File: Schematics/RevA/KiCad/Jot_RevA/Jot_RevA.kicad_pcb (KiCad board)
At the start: 4 copper layers, 37 x 62.6 mm, 83 parts, among them J1 USB-C, J2 Battery, Q1 AO3400A, Q2 AO3401A, Q3 AO3400A, Q4 AO3400A, Q5 AO3400A, Q6 AO3401A, Q7 AO3400A, Q8 AO3400A, SW1 SW_Push, U1 MDBT50Q-1MV2, U10 USBLC6-2SC6, U2 MMICT3902-00-012, U3 MMICT3902-00-012, U4 W25Q256JVEIQ, U5 MCP73831T-2ACI/OT, U6 MAX17048, U7 LIS2DW12TR, U8 DRV2605LDGS, U9 TPS7A0233, Y1 32.768kHz

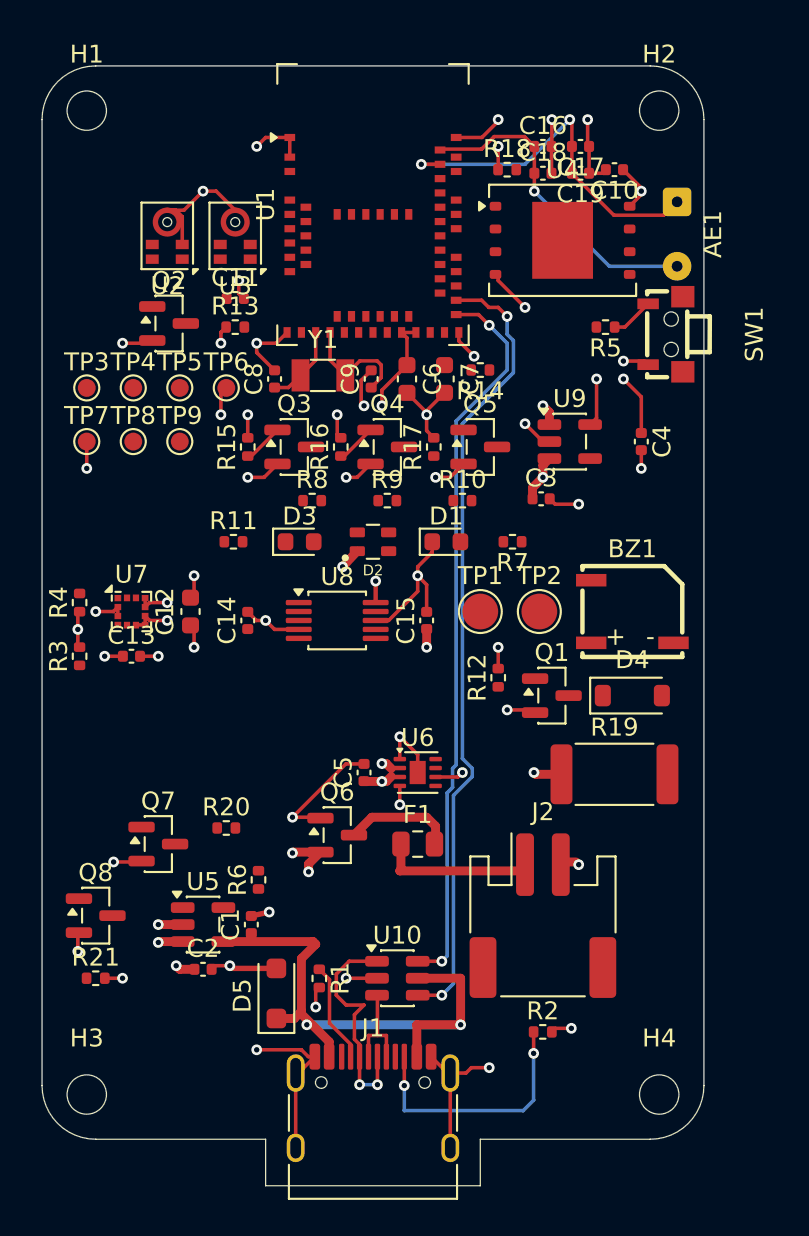
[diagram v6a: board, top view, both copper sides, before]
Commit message: Rev A layout complete: final routing and layout review fixes
- J2 is now two solder-wire holes (battery leads soldered): the JST-PH
  side-entry header is 5.5 mm tall and would not fit the 12.8 mm case.
  Removed from the JLCPCB BOM; BOM, architecture doc and case notes updated.
- LED drive pins re-assigned to match the transistor order:
  P1.08 red, P0.11 green, P0.12 blue. Pin list updated.
- No via drilled inside an SMD pad; no top-layer signal or via beside the
  crystal; 5 V branch removed from the power layer under the USB pair.
- R19 off the battery, C11 next to the mic, short ground vias at the
  module and decoupling capacitors, clean reset route.
- Silkscreen labels at 1.0 mm, battery + / - marked; zones refilled.
- DRC clean, board matches schematic, ERC clean.
- Case: 0.4 mm pocket over SW1, lip 0.8 mm.
- Architecture draft 7.
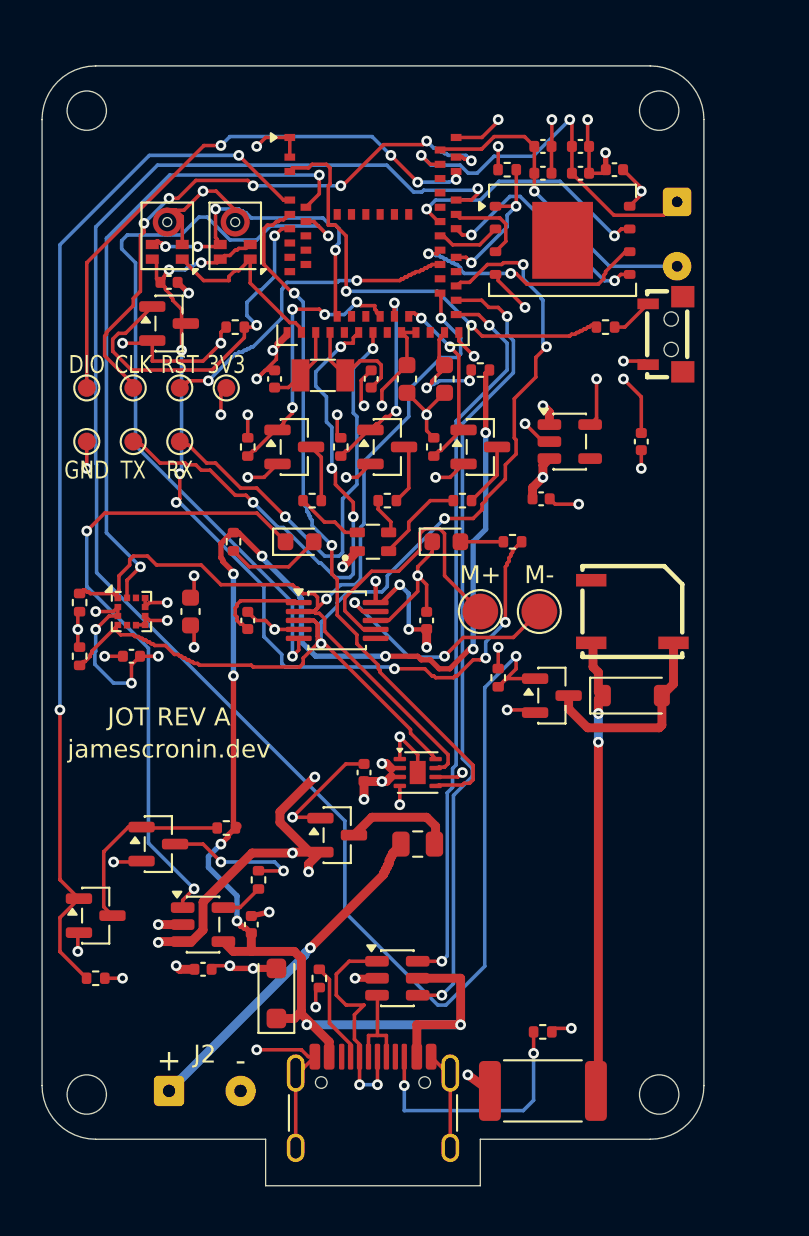
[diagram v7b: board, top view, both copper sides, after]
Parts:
- J2: value Battery -> Battery wires; footprint Connector_JST:JST_PH_S2B-PH-SM4-TB_1x02-1MP_P2.00mm_Horizontal -> Connector_Wire:SolderWire-0.15sqmm_1x02_P4mm_D0.5mm_OD1.5mm
- moved J2 23.1 mm to (88.6, 127.3)
- moved R19 18.1 mm to (109.5, 127.3)
- moved C11 3.81 mm to (88.6, 82.1)
- turned R11 to 90 degrees
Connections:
- U1 pad 25: LED_B -> LED_R
- U1 pad 27: LED_R -> LED_G
- U1 pad 29: LED_G -> LED_B
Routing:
- net BUZZER_PWM: track 0.00 -> 102.5 mm, vias 0 -> 2
- net I2C_SDA: track 0.00 -> 65.7 mm, vias 0 -> 4
- net VBUS: track 32.4 -> 91.2 mm, vias 2 -> 10
- net CHG_INHIBIT: track 0.00 -> 58.5 mm, vias 0 -> 2
- net I2C_SCL: track 0.00 -> 55.0 mm, vias 0 -> 2
- net /Audio/MIC_VDD: track 0.00 -> 51.7 mm, vias 0 -> 8
- net HAPTIC_EN: track 0.00 -> 43.1 mm, vias 0 -> 2
- net FG_ALRT: track 0.00 -> 39.7 mm, vias 0 -> 2
- net ACC_INT1: track 0.00 -> 36.7 mm, vias 0 -> 2
- net Net-(D3-K): track 0.00 -> 36.0 mm, vias 0 -> 2
- net SWDCLK: track 0.00 -> 32.6 mm, vias 0 -> 6
- net SWDIO: track 0.00 -> 32.2 mm, vias 0 -> 4
- net UART_TX: track 0.00 -> 31.2 mm, vias 0 -> 4
- net Net-(BZ1-+): track 0.00 -> 25.5 mm, vias 0 -> 2
- net BTN: track 0.00 -> 25.4 mm, vias 0 -> 2
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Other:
- board text added: "+"
- board text added: "-"
- board text added: "3V3"
- board text added: "CLK"
- board text added: "DIO"
- board text added: "GND"
- board text added: "JOT REV A"
- board text added: "M+"
- board text added: "M-"
- board text added: "RST"
- board text added: "RX"
- board text added: "TX"
- board text added: "jamescronin.dev"
